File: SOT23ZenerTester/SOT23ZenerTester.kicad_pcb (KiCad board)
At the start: 4 copper layers, 135 x 108 mm, 81 parts, among them J1 PJ-102AH, J2 282837-4, J3 L17HTHAS4F1C, J4 282837-3, J5 CSD_Dual_SOT23, J6 CSD_Dual_SOT23, J7 CSD_Dual_SOT23, J8 CSD_Dual_SOT23, J9 CSD_Dual_SOT23, Q1 PDTC123JT, Q10 PDTC123JT, Q11 PDTC123JT, Q12 PDTC123JT, Q13 PDTC123JT, Q14 PDTC123JT, Q15 PDTC123JT, Q2 PDTC123JT, Q3 PDTC123JT, Q4 PDTC123JT, Q5 PDTC123JT, Q6 PDTC123JT, Q7 PDTC123JT, Q8 PDTC123JT, Q9 PDTC123JT

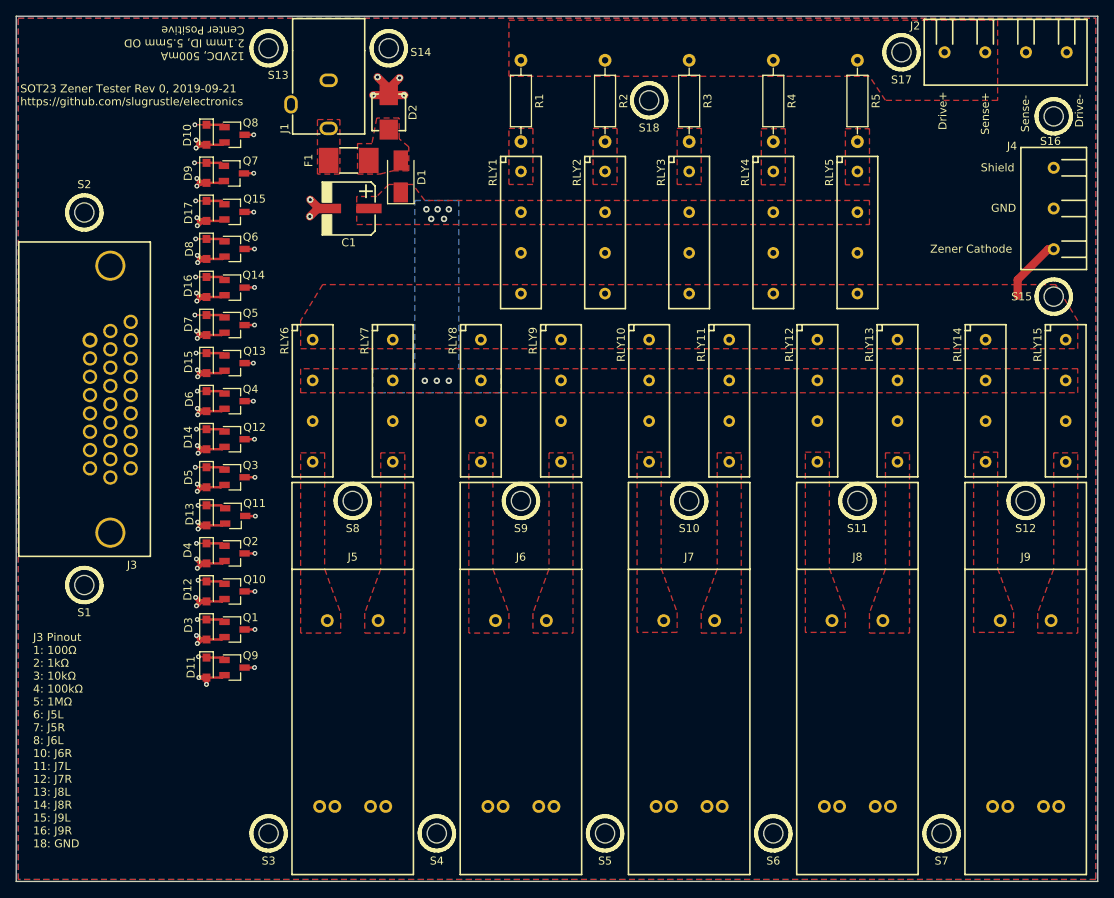
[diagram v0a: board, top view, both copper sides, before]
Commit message: SOT23 Zener Tester Rev1
Fixing footprints of J2 and J4.
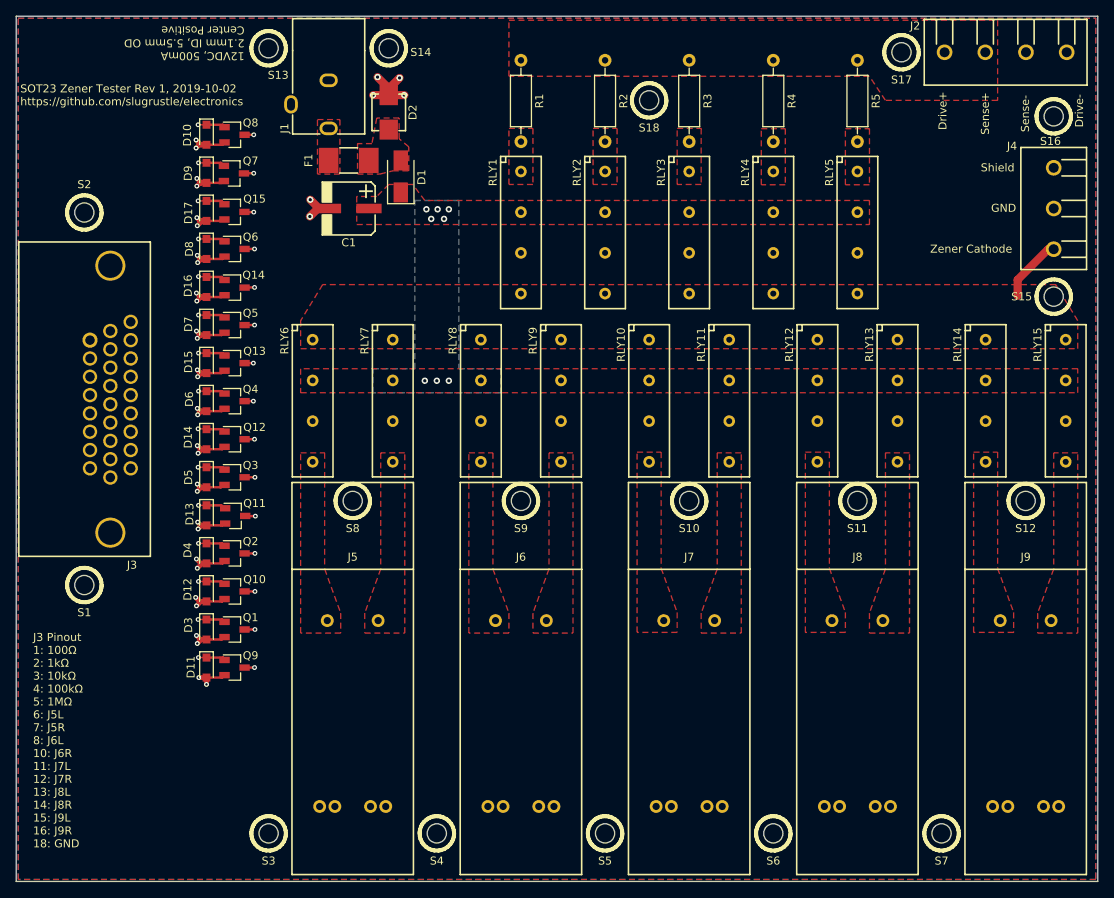
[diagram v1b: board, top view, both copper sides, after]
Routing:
- net /ZD5RLY: track 23.1 -> 28.5 mm
- net /ZD10RLY: track 32.3 -> 34.1 mm
- net /ZD3RLY: track 35.7 -> 37.2 mm
- net /ZD4RLY: track 30.4 -> 31.9 mm
- net /ZD6RLY: track 20.0 -> 21.5 mm
- net /R100RLY: track 28.1 -> 29.5 mm
- net /ZD9RLY: track 25.7 -> 27.0 mm
- net /ZD1RLY: track 26.6 -> 27.9 mm
- net /ZD8RLY: track 18.2 -> 19.5 mm
- net /R1MRLY: track 19.7 -> 20.9 mm
- net /R1KRLY: track 21.4 -> 22.6 mm
- net /ZD2RLY: track 33.8 -> 34.7 mm
- net /R10KRLY: track 14.8 -> 15.4 mm
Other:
- board text added: "SOT23 Zener Tester Rev 1, 2019-10-02 https://github.com/slugrustle/electronics"
- board text removed: "SOT23 Zener Tester Rev 0, 2019-09-21 https://github.com/slugrustle/electronics"
